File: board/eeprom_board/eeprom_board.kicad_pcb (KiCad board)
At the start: 2 copper layers, 30.5 x 12.7 mm, 6 parts, among them J1 Conn_01x04_Pin, U1 AT24C02C-SSHM-T, U2 AT24C32D-SSHM-T

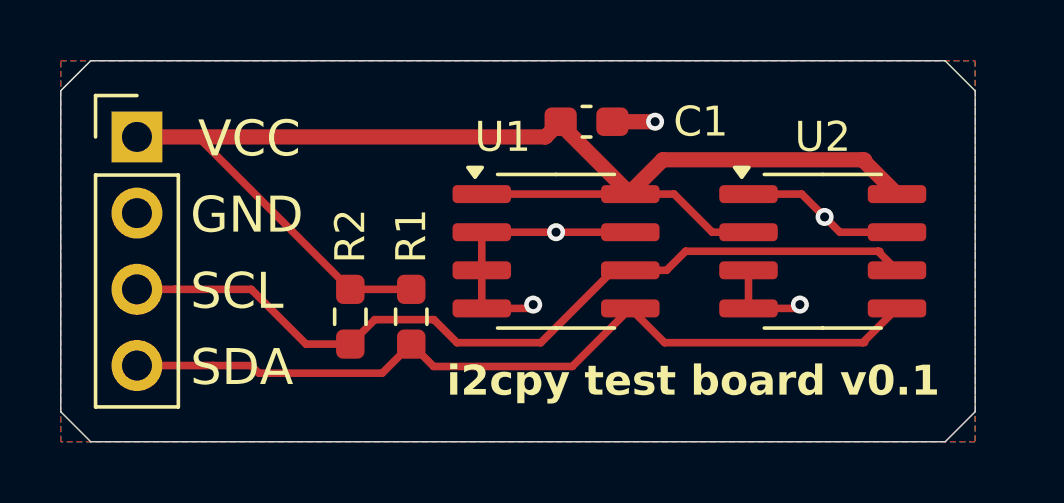
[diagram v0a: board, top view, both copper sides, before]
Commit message: Check ACK from device
Check the acks received from device to test i2c device presence.
No ack no device present.
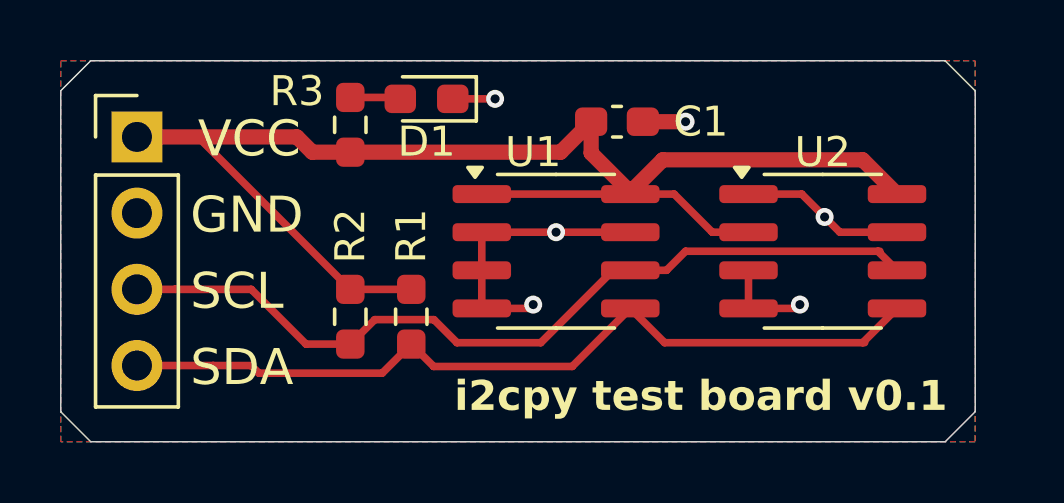
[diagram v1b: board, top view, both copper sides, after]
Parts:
- added D1: LED, LED_SMD:LED_0603_1608Metric_Pad1.05x0.95mm_HandSolder, F.Cu at (97.3, 77.5)
- added R3: 1K, Resistor_SMD:R_0603_1608Metric_Pad0.98x0.95mm_HandSolder, F.Cu at (94.7, 78.3)
- moved C1 1.02 mm to (103.6, 78.2)
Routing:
- net Net-(D1-A): track 0.00 -> 1.89 mm
- net GND: track 19.0 -> 20.4 mm, vias 5 -> 6
- net VCC: track 48.2 -> 49.2 mm
